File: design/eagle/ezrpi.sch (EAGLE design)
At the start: 27 parts

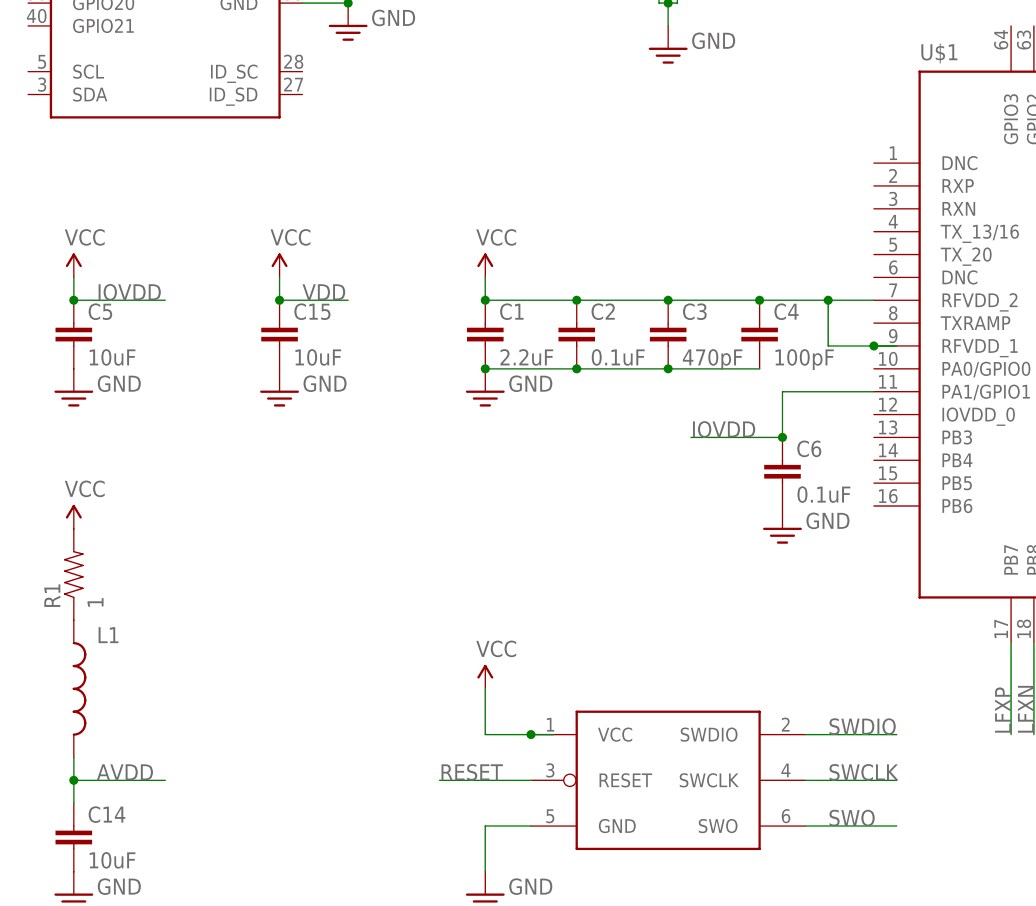
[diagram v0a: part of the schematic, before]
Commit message: rebranded project to generic EZRPi sub-GHz HAT
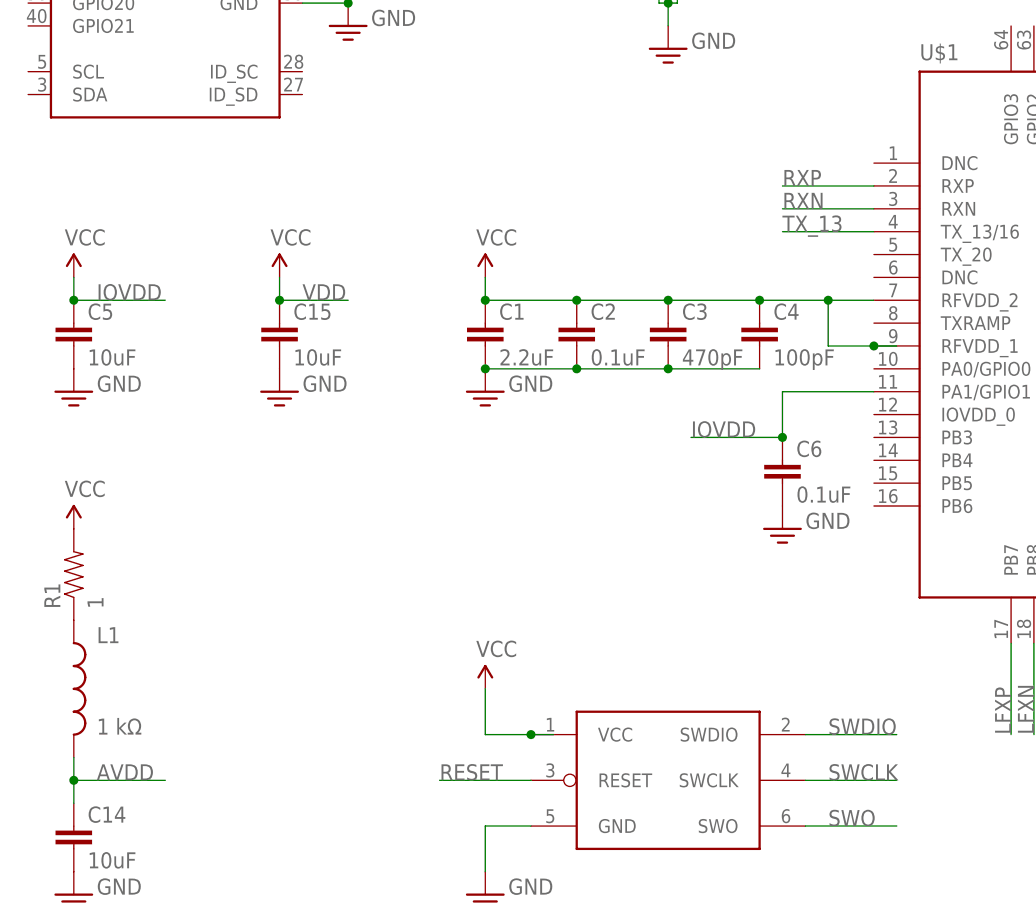
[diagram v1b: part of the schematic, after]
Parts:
- L1: value (none) -> 1 kΩ
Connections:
- new net RXN: U$1.RXN
- new net RXP: U$1.RXP
- new net TX_13: U$1.TX_13/16
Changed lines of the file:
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@@
 <schematic xreflabel="%F%N/%S.%C%R" xrefpart="/%S.%C%R">
 <attributes>
-<attribute name="CNAME" value="Dash7 Raspberry Pi HAT"/>
+<attribute name="CNAME" value="EZRPi sub-GHz Raspberry Pi HAT"/>
 <attribute name="CREVISION" value="1.0"/>
 <attribute name="DESIGNER" value="Christophe VG"/>
@@
 <part name="C13" library="passive" deviceset="CAP" device="0805" value="10nF"/>
 <part name="R1" library="passive" deviceset="RESISTOR" device="0805-RES" value="1"/>
-<part name="L1" library="passive" deviceset="INDUCTOR" device="0805"/>
+<part name="L1" library="passive" deviceset="INDUCTOR" device="0805" value="1 kΩ"/>
 <part name="C14" library="passive" deviceset="CAP" device="0805" value="10uF"/>
 <part name="GND-ISO13" library="setup" deviceset="GND" device=""/>
@@
 </segment>
 </net>
+<net name="RXP" class="0">
+<segment>
+<pinref part="U$1" gate="G$1" pin="RXP"/>
+<wire x1="124.46" y1="12.7" x2="114.3" y2="12.7" width="0.1524" layer="91"/>
+<label x="114.3" y="12.7" size="1.778" layer="95"/>
+</segment>
+</net>
+<net name="RXN" class="0">
+<segment>
+<pinref part="U$1" gate="G$1" pin="RXN"/>
+<wire x1="124.46" y1="10.16" x2="114.3" y2="10.16" width="0.1524" layer="91"/>
+<label x="114.3" y="10.16" size="1.778" layer="95"/>
+</segment>
+</net>
+<net name="TX_13" class="0">
+<segment>
+<pinref part="U$1" gate="G$1" pin="TX_13/16"/>
+<wire x1="124.46" y1="7.62" x2="114.3" y2="7.62" width="0.1524" layer="91"/>
+<label x="114.3" y="7.62" size="1.778" layer="95"/>
+</segment>
+</net>

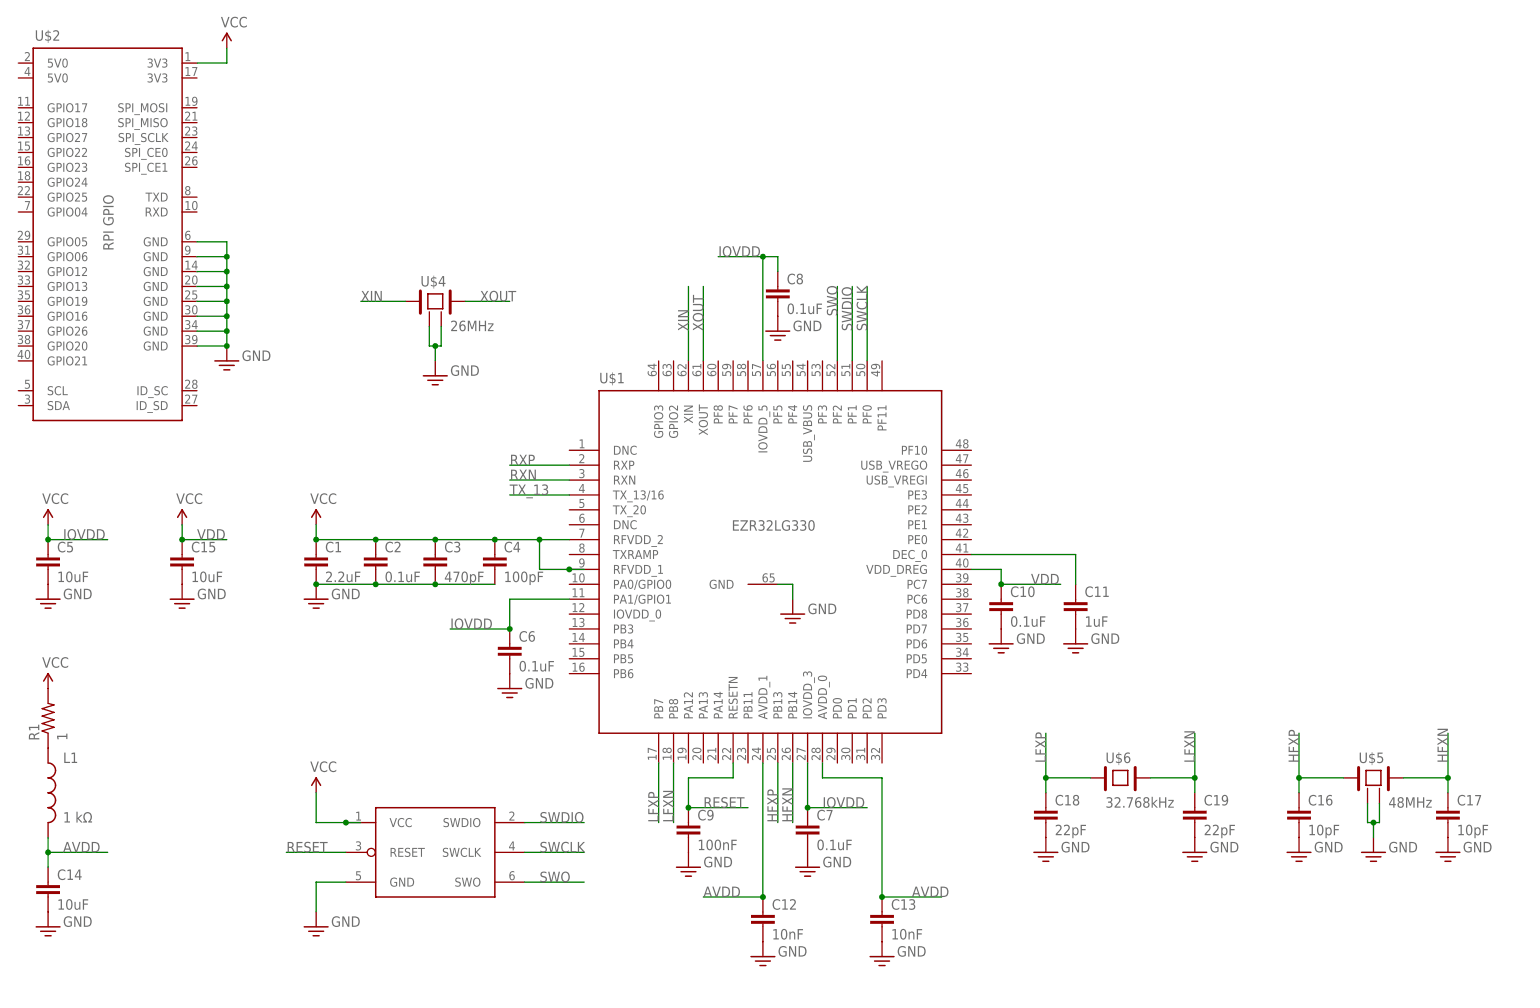
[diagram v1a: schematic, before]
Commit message: completed schematic, started work on board design
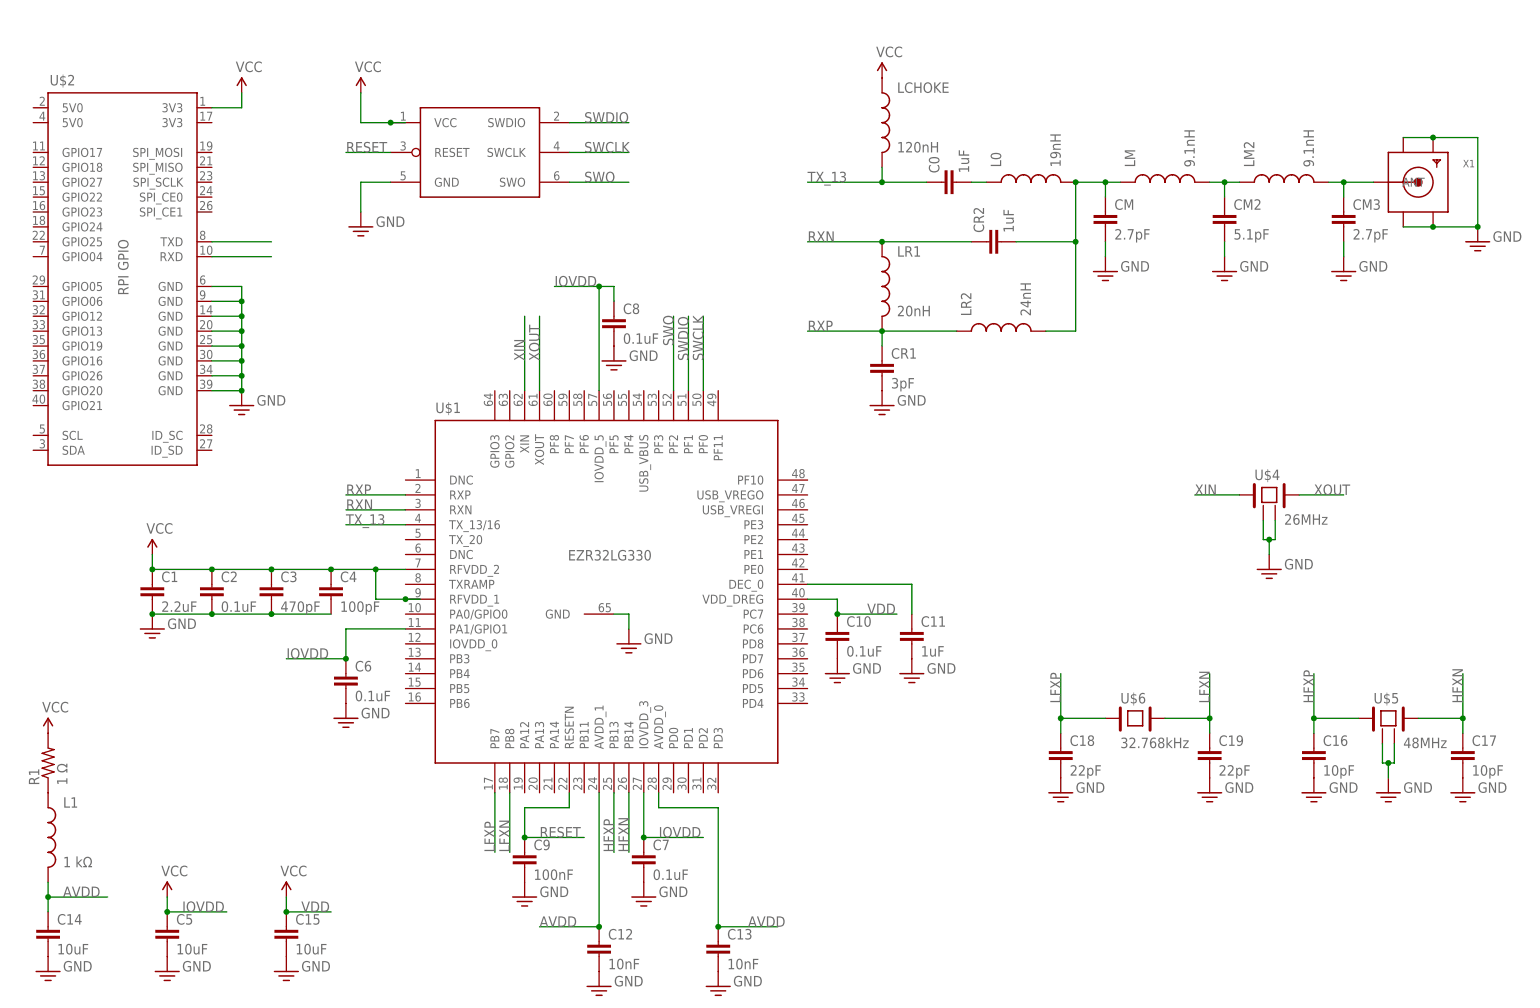
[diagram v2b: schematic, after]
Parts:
- added C0, CR2: 1uF, passive:CAP0805
- added CM, CM3: 2.7pF, passive:CAP0805
- added CM2: 5.1pF, passive:CAP0805
- added CR1: 3pF, passive:CAP0805
- added L0: 19nH, passive:INDUCTOR0402
- added LCHOKE: 120nH, passive:INDUCTOR0805
- added LM, LM2: 9.1nH, passive:INDUCTOR0805
- added LR1: 20nH, passive:INDUCTOR0805
- added LR2: 24nH, passive:INDUCTOR0805
- added X1: (no value), connector:SMACONNECTOR
- R1: value 1 -> 1 Ω
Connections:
- removed net GND-ISO: C1.2, C10.2, C11.2, C12.2, C13.2, C14.2, C15.2, C16.2, C17.2, C18.2, C19.2, C2.2, C3.2, C4.2, C5.2, C6.2, C7.2, C8.2, C9.2, U$1.GND, U$2.GND@1, U$2.GND@2, U$2.GND@3, U$2.GND@4, U$2.GND@5, U$2.GND@6, U$2.GND@7, U$2.GND@8, U$3.GND, U$4.GND@2, U$4.GND@4, U$5.GND@2, U$5.GND@4
- new net GND: C1.2, C10.2, C11.2, C12.2, C13.2, C14.2, C15.2, C16.2, C17.2, C18.2, C19.2, C2.2, C3.2, C4.2, C5.2, C6.2, C7.2, C8.2, C9.2, CM.2, CM2.2, CM3.2, CR1.2, U$1.GND, U$2.GND@1, U$2.GND@2, U$2.GND@3, U$2.GND@4, U$2.GND@5, U$2.GND@6, U$2.GND@7, U$2.GND@8, U$3.GND, U$4.GND@2, U$4.GND@4, U$5.GND@2, U$5.GND@4, X1.GND1, X1.GND2, X1.GND3, X1.GND4
- new net N$1: CM3.1, LM2.2, X1.ANT
- new net N$3: CM2.1, LM.2, LM2.1
- new net N$5: U$2.TXD
- new net N$6: C0.2, L0.1
- new net N$7: CM.1, CR2.2, L0.2, LM.1, LR2.2
- new net N$8: U$2.RXD
- net RXN: now also CR2.1, LR1.1
- net RXP: now also CR1.1, LR1.2, LR2.1
- net TX_13: now also C0.1, LCHOKE.2
- net VCC: now also LCHOKE.1
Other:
- moved on the sheet: C1, C10, C11, C12, C13, C14, C15, C16, C17, C18, C19, C2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

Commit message: completed schematic and first board layout
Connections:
- removed net N$5: U$2.TXD
- removed net N$8: U$2.RXD
- new net RX: U$1.PE1, U$2.TXD
- new net TX: U$1.PE0, U$2.RXD
- net LFXN: now also C18.1, U$6.1; no longer C19.1, U$6.2
- net LFXP: now also C19.1, U$6.2; no longer C18.1, U$6.1
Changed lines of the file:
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@@
 <grid distance="0.1" unitdist="inch" unit="inch" style="lines" multiple="1" display="no" altdistance="0.01" altunitdist="inch" altunit="inch"/>
 <layers>
-<layer number="1" name="Top" color="4" fill="1" visible="yes" active="no"/>
-<layer number="16" name="Bottom" color="1" fill="1" visible="yes" active="no"/>
-<layer number="17" name="Pads" color="2" fill="1" visible="yes" active="no"/>
-<layer number="18" name="Vias" color="2" fill="1" visible="yes" active="no"/>
-<layer number="19" name="Unrouted" color="6" fill="1" visible="yes" active="no"/>
-<layer number="20" name="Dimension" color="15" fill="1" visible="yes" active="no"/>
-<layer number="21" name="tPlace" color="7" fill="1" visible="yes" active="no"/>
-<layer number="22" name="bPlace" color="7" fill="1" visible="yes" active="no"/>
-<layer number="23" name="tOrigins" color="15" fill="1" visible="yes" active="no"/>
-<layer number="24" name="bOrigins" color="15" fill="1" visible="yes" active="no"/>
-<layer number="25" name="tNames" color="7" fill="1" visible="yes" active="no"/>
-<layer number="26" name="bNames" color="7" fill="1" visible="yes" active="no"/>
-<layer number="27" name="tValues" color="7" fill="1" visible="yes" active="no"/>
-<layer number="28" name="bValues" color="7" fill="1" visible="yes" active="no"/>
+<layer number="1" name="Top" color="4" fill="1" visible="no" active="no"/>
+<layer number="16" name="Bottom" color="1" fill="1" visible="no" active="no"/>
+<layer number="17" name="Pads" color="2" fill="1" visible="no" active="no"/>
+<layer number="18" name="Vias" color="2" fill="1" visible="no" active="no"/>
+<layer number="19" name="Unrouted" color="6" fill="1" visible="no" active="no"/>
+<layer number="20" name="Dimension" color="15" fill="1" visible="no" active="no"/>
+<layer number="21" name="tPlace" color="7" fill="1" visible="no" active="no"/>
+<layer number="22" name="bPlace" color="7" fill="1" visible="no" active="no"/>
+<layer number="23" name="tOrigins" color="15" fill="1" visible="no" active="no"/>
+<layer number="24" name="bOrigins" color="15" fill="1" visible="no" active="no"/>
+<layer number="25" name="tNames" color="7" fill="1" visible="no" active="no"/>
+<layer number="26" name="bNames" color="7" fill="1" visible="no" active="no"/>
+<layer number="27" name="tValues" color="7" fill="1" visible="no" active="no"/>
+<layer number="28" name="bValues" color="7" fill="1" visible="no" active="no"/>
 <layer number="29" name="tStop" color="7" fill="3" visible="no" active="no"/>
 <layer number="30" name="bStop" color="7" fill="6" visible="no" active="no"/>
@@
 <layer number="35" name="tGlue" color="7" fill="4" visible="no" active="no"/>
 <layer number="36" name="bGlue" color="7" fill="5" visible="no" active="no"/>
-<layer number="37" name="tTest" color="7" fill="1" visible="yes" active="no"/>
-<layer number="38" name="bTest" color="7" fill="1" visible="yes" active="no"/>
+<layer number="37" name="tTest" color="7" fill="1" visible="no" active="no"/>
+<layer number="38" name="bTest" color="7" fill="1" visible="no" active="no"/>
 <layer number="39" name="tKeepout" color="4" fill="11" visible="no" active="no"/>
 <layer number="40" name="bKeepout" color="1" fill="11" visible="no" active="no"/>
@@
 <layer number="44" name="Drills" color="7" fill="1" visible="no" active="no"/>
 <layer number="45" name="Holes" color="7" fill="1" visible="no" active="no"/>
-<layer number="46" name="Milling" color="3" fill="1" visible="yes" active="no"/>
-<layer number="47" name="Measures" color="7" fill="1" visible="yes" active="no"/>
-<layer number="48" name="Document" color="7" fill="1" visible="yes" active="no"/>
-<layer number="49" name="Reference" color="7" fill="1" visible="yes" active="no"/>
-<layer number="50" name="dxf" color="7" fill="1" visible="yes" active="no"/>
-<layer number="51" name="tDocu" color="7" fill="1" visible="yes" active="no"/>
-<layer number="52" name="bDocu" color="7" fill="1" visible="yes" active="no"/>
-<layer number="53" name="tGND_GNDA" color="7" fill="9" visible="yes" active="no"/>
-<layer number="54" name="bGND_GNDA" color="1" fill="9" visible="yes" active="no"/>
-<layer number="56" name="wert" color="7" fill="1" visible="yes" active="no"/>
-<layer number="57" name="tCAD" color="7" fill="1" visible="yes" active="no"/>
-<layer number="59" name="tCarbon" color="7" fill="1" visible="yes" active="no"/>
-<layer number="60" name="bCarbon" color="7" fill="1" visible="yes" active="no"/>
+<layer number="46" name="Milling" color="3" fill="1" visible="no" active="no"/>
+<layer number="47" name="Measures" color="7" fill="1" visible="no" active="no"/>
+<layer number="48" name="Document" color="7" fill="1" visible="no" active="no"/>
+<layer number="49" name="Reference" color="7" fill="1" visible="no" active="no"/>
+<layer number="50" name="dxf" color="7" fill="1" visible="no" active="no"/>
+<layer number="51" name="tDocu" color="7" fill="1" visible="no" active="no"/>
+<layer number="52" name="bDocu" color="7" fill="1" visible="no" active="no"/>
+<layer number="53" name="tGND_GNDA" color="7" fill="9" visible="no" active="no"/>
+<layer number="54" name="bGND_GNDA" color="1" fill="9" visible="no" active="no"/>
+<layer number="56" name="wert" color="7" fill="1" visible="no" active="no"/>
+<layer number="57" name="tCAD" color="7" fill="1" visible="no" active="no"/>
+<layer number="59" name="tCarbon" color="7" fill="1" visible="no" active="no"/>
+<layer number="60" name="bCarbon" color="7" fill="1" visible="no" active="no"/>
 <layer number="90" name="Modules" color="5" fill="1" visible="yes" active="yes"/>
 <layer number="91" name="Nets" color="2" fill="1" visible="yes" active="yes"/>
@@
 <net name="LFXP" class="0">
 <segment>
-<pinref part="U$6" gate="G$1" pin="1"/>
-<pinref part="C18" gate="G$1" pin="1"/>
-<wire x1="215.9" y1="-30.48" x2="208.28" y2="-30.48" width="0.1524" layer="91"/>
-<wire x1="208.28" y1="-30.48" x2="208.28" y2="-33.02" width="0.1524" layer="91"/>
-<wire x1="208.28" y1="-30.48" x2="208.28" y2="-22.86" width="0.1524" layer="91"/>
-<junction x="208.28" y="-30.48"/>
-<label x="208.28" y="-27.94" size="1.778" layer="95" rot="R90"/>
-</segment>
-<segment>
 <pinref part="U$1" gate="G$1" pin="PB7"/>
 <wire x1="111.76" y1="-43.18" x2="111.76" y2="-53.34" width="0.1524" layer="91"/>
 <label x="111.76" y="-53.34" size="1.778" layer="95" rot="R90"/>
 </segment>
-</net>
-<net name="LFXN" class="0">
-<segment>
+<segment>
+<pinref part="C19" gate="G$1" pin="1"/>
+<wire x1="233.68" y1="-33.02" x2="233.68" y2="-30.48" width="0.1524" layer="91"/>
 <pinref part="U$6" gate="G$1" pin="2"/>
-<pinref part="C19" gate="G$1" pin="1"/>
+<wire x1="233.68" y1="-30.48" x2="233.68" y2="-22.86" width="0.1524" layer="91"/>
 <wire x1="226.06" y1="-30.48" x2="233.68" y2="-30.48" width="0.1524" layer="91"/>
-<wire x1="233.68" y1="-30.48" x2="233.68" y2="-33.02" width="0.1524" layer="91"/>
-<wire x1="233.68" y1="-30.48" x2="233.68" y2="-22.86" width="0.1524" layer="91"/>
 <junction x="233.68" y="-30.48"/>
 <label x="233.68" y="-27.94" size="1.778" layer="95" rot="R90"/>
 </segment>
+</net>
+<net name="LFXN" class="0">
 <segment>
 <pinref part="U$1" gate="G$1" pin="PB8"/>
 <wire x1="114.3" y1="-43.18" x2="114.3" y2="-53.34" width="0.1524" layer="91"/>
 <label x="114.3" y="-53.34" size="1.778" layer="95" rot="R90"/>
+</segment>
+<segment>
+<pinref part="C18" gate="G$1" pin="1"/>
+<wire x1="208.28" y1="-33.02" x2="208.28" y2="-30.48" width="0.1524" layer="91"/>
+<pinref part="U$6" gate="G$1" pin="1"/>
+<wire x1="208.28" y1="-30.48" x2="208.28" y2="-22.86" width="0.1524" layer="91"/>
+<wire x1="215.9" y1="-30.48" x2="208.28" y2="-30.48" width="0.1524" layer="91"/>
+<junction x="208.28" y="-30.48"/>
+<label x="208.28" y="-27.94" size="1.778" layer="95" rot="R90"/>
 </segment>
 </net>
@@
 </segment>
 </net>
-<net name="N$5" class="0">
+<net name="RX" class="0">
 <segment>
 <pinref part="U$2" gate="G$1" pin="TXD"/>
 <wire x1="63.5" y1="50.8" x2="73.66" y2="50.8" width="0.1524" layer="91"/>
-</segment>
-</net>
-<net name="N$8" class="0">
+<label x="71.12" y="50.8" size="1.778" layer="95"/>
+</segment>
+<segment>
+<pinref part="U$1" gate="G$1" pin="PE1"/>
+<wire x1="165.1" y1="-2.54" x2="177.8" y2="-2.54" width="0.1524" layer="91"/>
+<label x="175.26" y="-2.54" size="1.778" layer="95"/>
+</segment>
+</net>
+<net name="TX" class="0">
 <segment>
 <pinref part="U$2" gate="G$1" pin="RXD"/>
 <wire x1="63.5" y1="48.26" x2="73.66" y2="48.26" width="0.1524" layer="91"/>
-</segment>
-</net>
+<label x="71.12" y="48.26" size="1.778" layer="95"/>
+</segment>
+<segment>
+<pinref part="U$1" gate="G$1" pin="PE0"/>
+<wire x1="165.1" y1="-5.08" x2="177.8" y2="-5.08" width="0.1524" layer="91"/>
+<label x="175.26" y="-5.08" size="1.778" layer="95"/>
+</segment>
+</net>

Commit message: fixed incorrect pin connection on IOVDD_0
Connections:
- net IOVDD: now also U$1.IOVDD_0; no longer U$1.PA1/GPIO1
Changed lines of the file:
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@@
 <net name="IOVDD" class="0">
 <segment>
-<pinref part="U$1" gate="G$1" pin="PA1/GPIO1"/>
 <pinref part="C6" gate="G$1" pin="1"/>
-<wire x1="96.52" y1="-15.24" x2="86.36" y2="-15.24" width="0.1524" layer="91"/>
-<wire x1="86.36" y1="-15.24" x2="86.36" y2="-20.32" width="0.1524" layer="91"/>
 <wire x1="86.36" y1="-20.32" x2="76.2" y2="-20.32" width="0.1524" layer="91"/>
+<label x="76.2" y="-20.32" size="1.778" layer="95"/>
+<pinref part="U$1" gate="G$1" pin="IOVDD_0"/>
+<wire x1="86.36" y1="-20.32" x2="86.36" y2="-17.78" width="0.1524" layer="91"/>
+<wire x1="86.36" y1="-17.78" x2="96.52" y2="-17.78" width="0.1524" layer="91"/>
 <junction x="86.36" y="-20.32"/>
-<label x="76.2" y="-20.32" size="1.778" layer="95"/>
 </segment>
 <segment>
